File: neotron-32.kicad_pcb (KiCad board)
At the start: 2 copper layers, 166.9 x 140.7 mm, 93 parts, among them J1 Conn_02x06, J10 micro SD Card, J11 Conn_02x13_Top_Bottom, J12 AVR-ISP-6, J13 DE9 Male, J14 DE9 Male, J15 Double-mini-DIN-6, J17 DB15HD_Female, J18 Conn_02x05, J2 Conn_02x06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

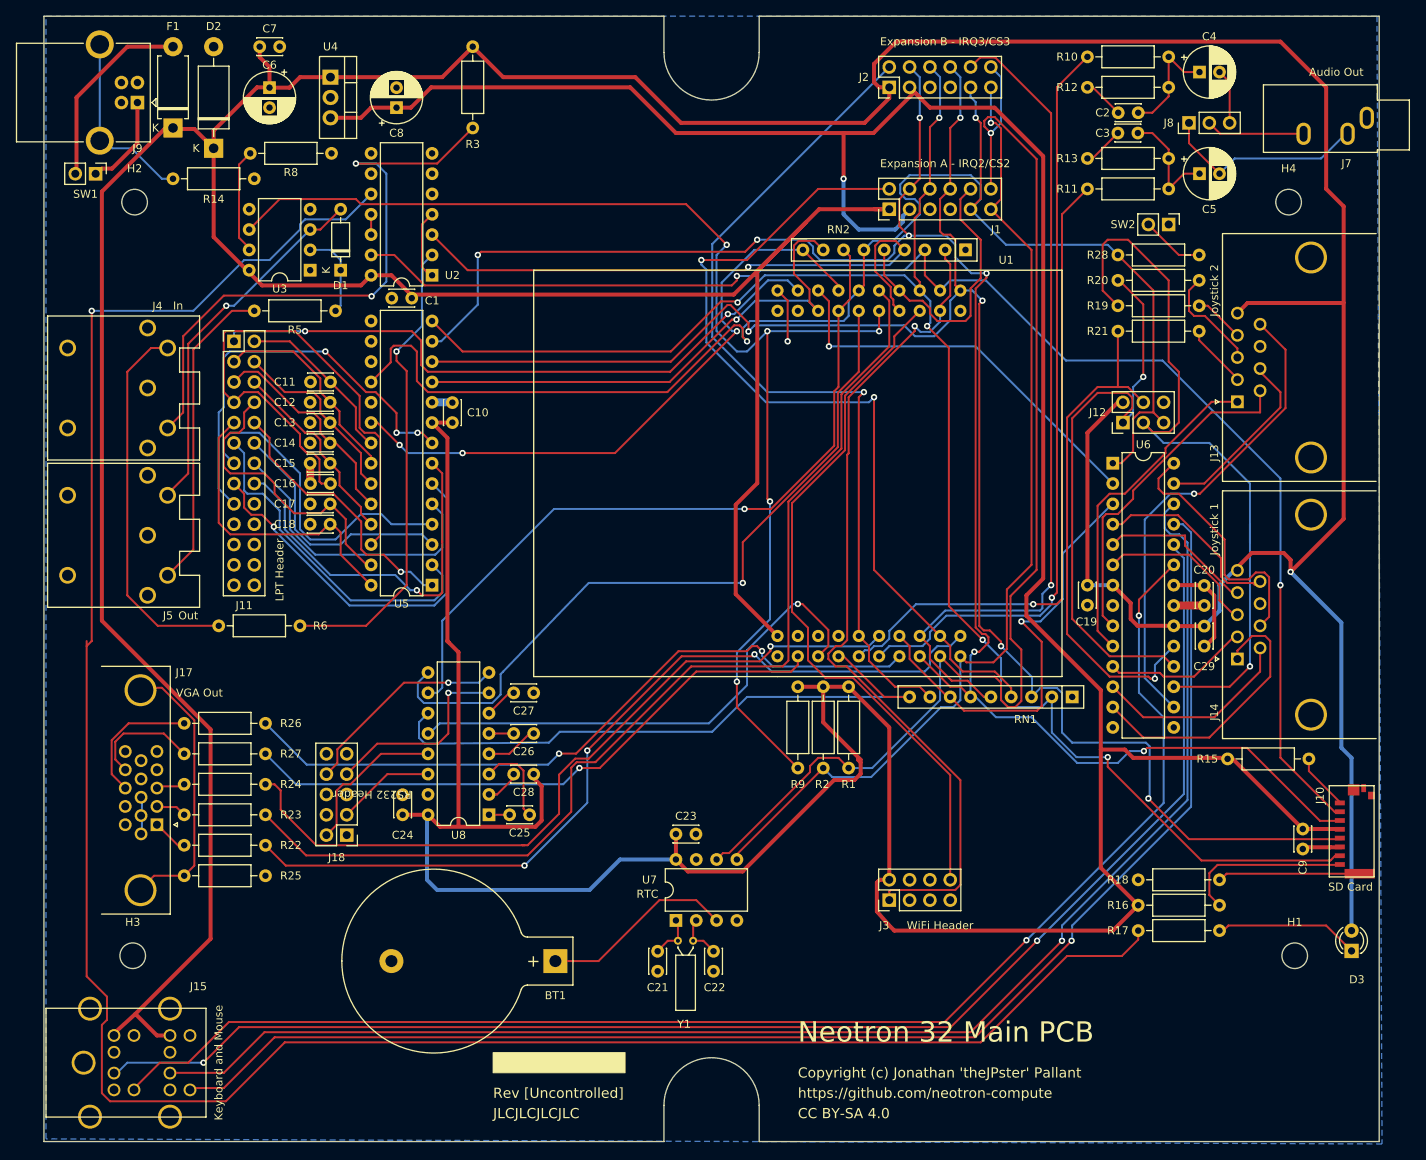
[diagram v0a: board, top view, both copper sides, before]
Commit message: Moved non-standard components into local libraries.
neotron-32.lib is the symbol library.
neotron-32.pretty is the footprint library.

Also swapped the DE9 and DB25 headers for IDC boxed versions. Involved
moving a resistor out of the way.

The Keystone 103 battery holder is a straight copy of the standard
footprint, but with the Courtyard removed to bypass the 'Courtyard is
not closed' DRC error.
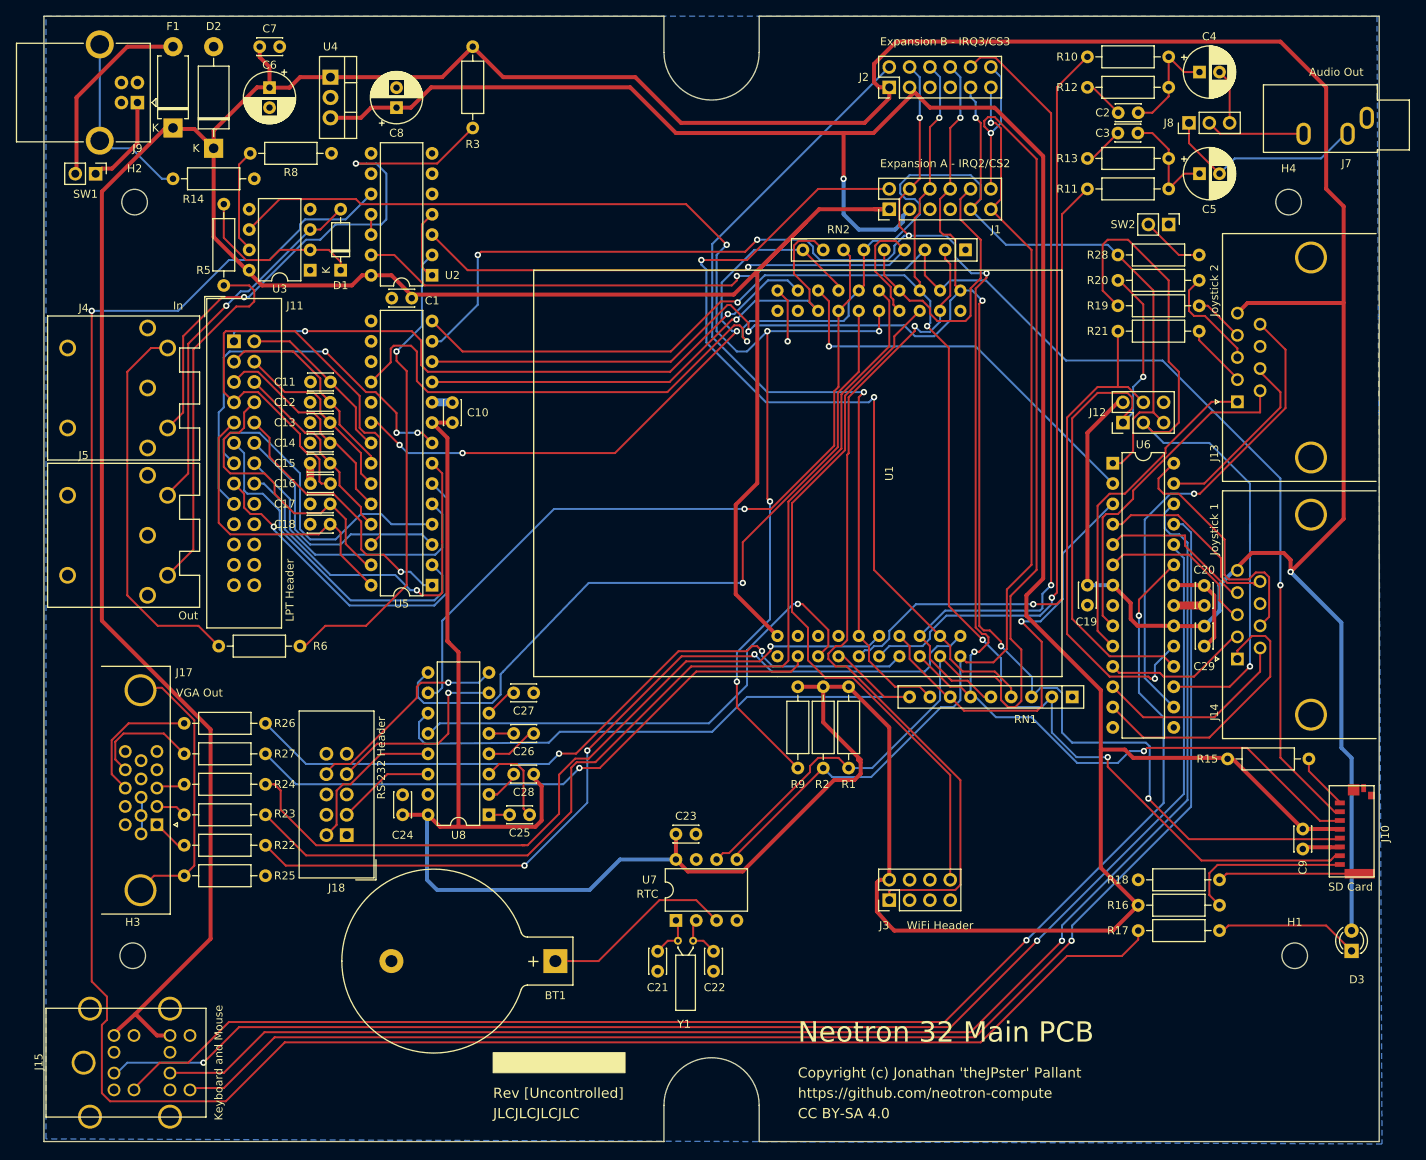
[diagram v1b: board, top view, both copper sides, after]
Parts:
- BT1: footprint JGP Footprints:BatteryHolder_Keystone_103_1x20mm -> Neotron 32:BatteryHolder_Keystone_103_1x20mm
- J10: footprint JGP Footprints:Molex_4730_2651 -> Neotron 32:Molex_4730_2651
- J11: footprint Connector_PinHeader_2.54mm:PinHeader_2x13_P2.54mm_Vertical -> Connector_IDC:IDC-Header_2x13_P2.54mm_Vertical
- J15: footprint JGP Footprints:Double_mini-DIN_6 -> Neotron 32:Double_mini-DIN_6
- J18: footprint Connector_PinHeader_2.54mm:PinHeader_2x05_P2.54mm_Vertical -> Connector_IDC:IDC-Header_2x05_P2.54mm_Vertical
- J4, J5: footprint JGP Footprints:5P180 DIN Socket -> Neotron 32:5P180_DIN_Socket
- U1: footprint JGP Footprints:Launchpad_4x10 -> Neotron 32:Launchpad_4x10
- moved R5 19.3 mm to (93.3, 41.3), turned to 270 degrees
- moved R6 2.54 mm to (102.9, 96.5)
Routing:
- net Net-(D1-Pad1): track 10.9 -> 22.2 mm
- net Net-(J5-Pad4): track 39.2 -> 45.1 mm
- net Net-(J4-Pad4): track 74.7 -> 70.1 mm
- net Net-(R17-Pad2): track 280.8 -> 279.6 mm
- net Net-(J4-Pad5): track 47.2 -> 48.3 mm
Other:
- board text added: "RS-232 Header"
- board text removed: "RS232 Header"

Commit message: Add a push button power switch.
Also moved reset into the corner and tidied up a few tracks.
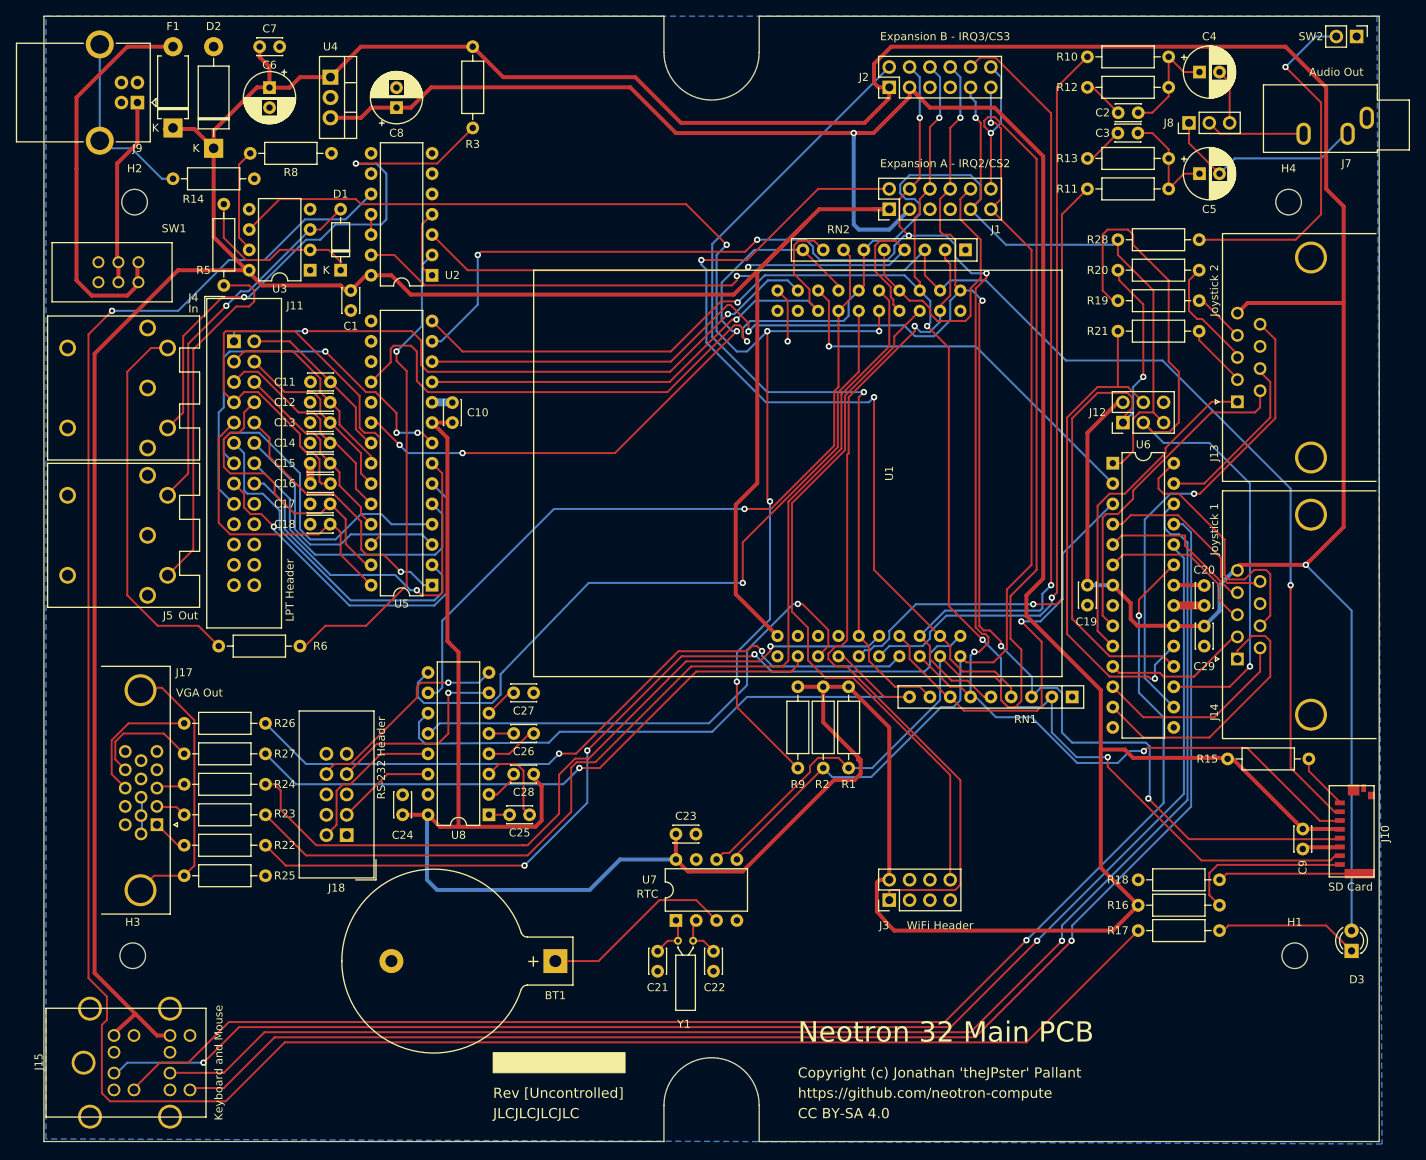
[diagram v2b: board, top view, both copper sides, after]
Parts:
- SW1: value SW_SPST -> SW_Push_DPDT; footprint Connector_PinHeader_2.54mm:PinHeader_1x02_P2.54mm_Vertical -> Neotron 32:PHB2UEETS1A
- moved SW2 33.2 mm to (234.9, 20.3)
- moved SW1 12.5 mm to (79.4, 49.8), turned to 0 degrees
- moved C1 7.68 mm to (109.2, 52.1), turned to 270 degrees
- moved R28 1.91 mm to (205.1, 45.7)
- moved R20 1.27 mm to (215.3, 49.5)
- moved R19 0.63 mm to (215.3, 53.3)
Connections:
- SW1 pad 1: Net-(J9-Pad1) -> (no net)
- SW1 pad 2: Net-(F1-Pad2) -> Net-(J9-Pad1)
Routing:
- net Net-(R28-Pad2): track 7.93 -> 44.7 mm, vias 0 -> 1
- net Net-(F1-Pad2): track 24.9 -> 50.0 mm
- net +5V: track 658.1 -> 641.0 mm
- net Net-(J9-Pad1): track 11.7 -> 23.6 mm
- net GND: track 45.1 -> 36.4 mm
- net /Keyboard, Mouse and Joystick/AT_SCK: track 94.9 -> 97.5 mm
- net Net-(R17-Pad2): track 279.6 -> 277.5 mm
- net /~RESET: track 183.6 -> 185.2 mm
- net +3V3: track 496.4 -> 497.9 mm
- net /Keyboard, Mouse and Joystick/AT_MISO: track 71.5 -> 72.7 mm
- net /Keyboard, Mouse and Joystick/SELECT_JS2: track 22.8 -> 21.7 mm
- net /Keyboard, Mouse and Joystick/START_C_JS2: track 60.1 -> 59.1 mm
- net /Keyboard, Mouse and Joystick/LEFT_GND_JS2: track 13.5 -> 14.3 mm
- net /Keyboard, Mouse and Joystick/SELECT_JS1: track 32.2 -> 32.9 mm

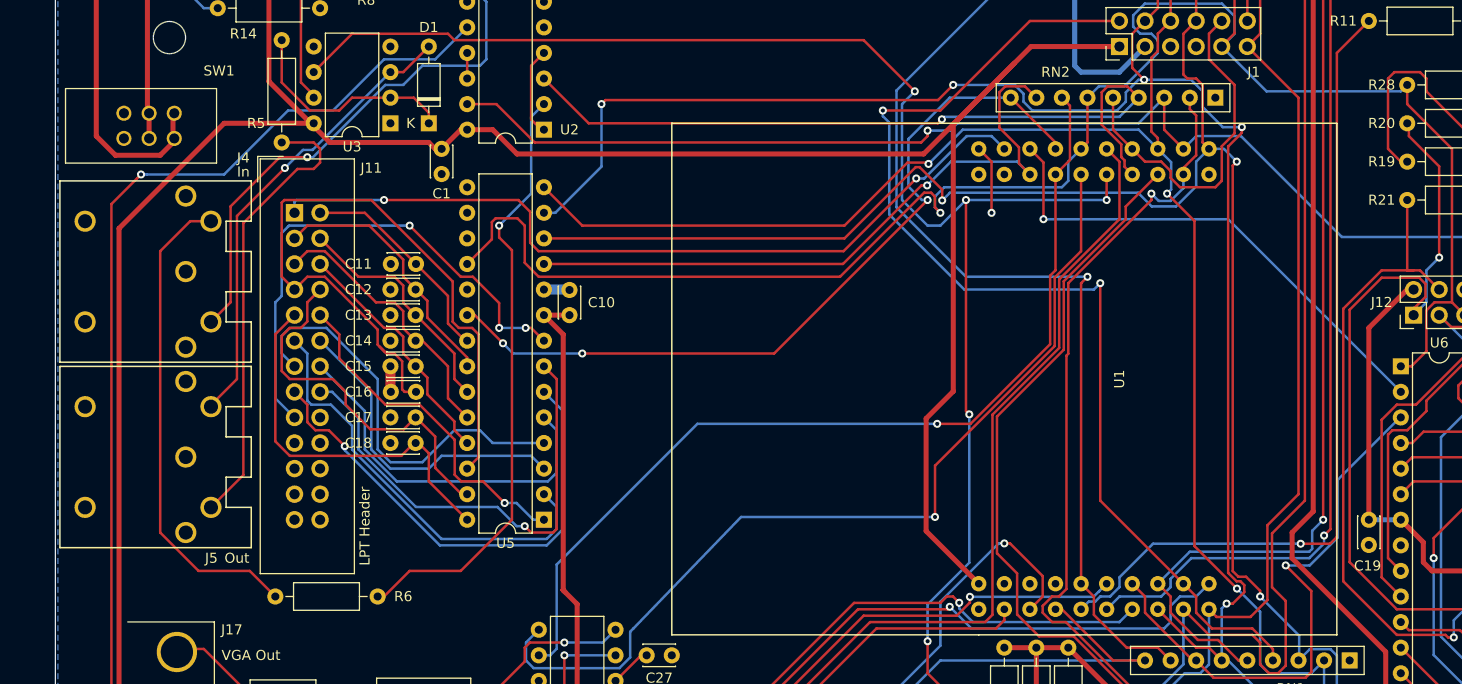
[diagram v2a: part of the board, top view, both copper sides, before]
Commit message: Fixed spacing between MIDI connectors.
Also tidied up some more tracks and re-aligned end panel.
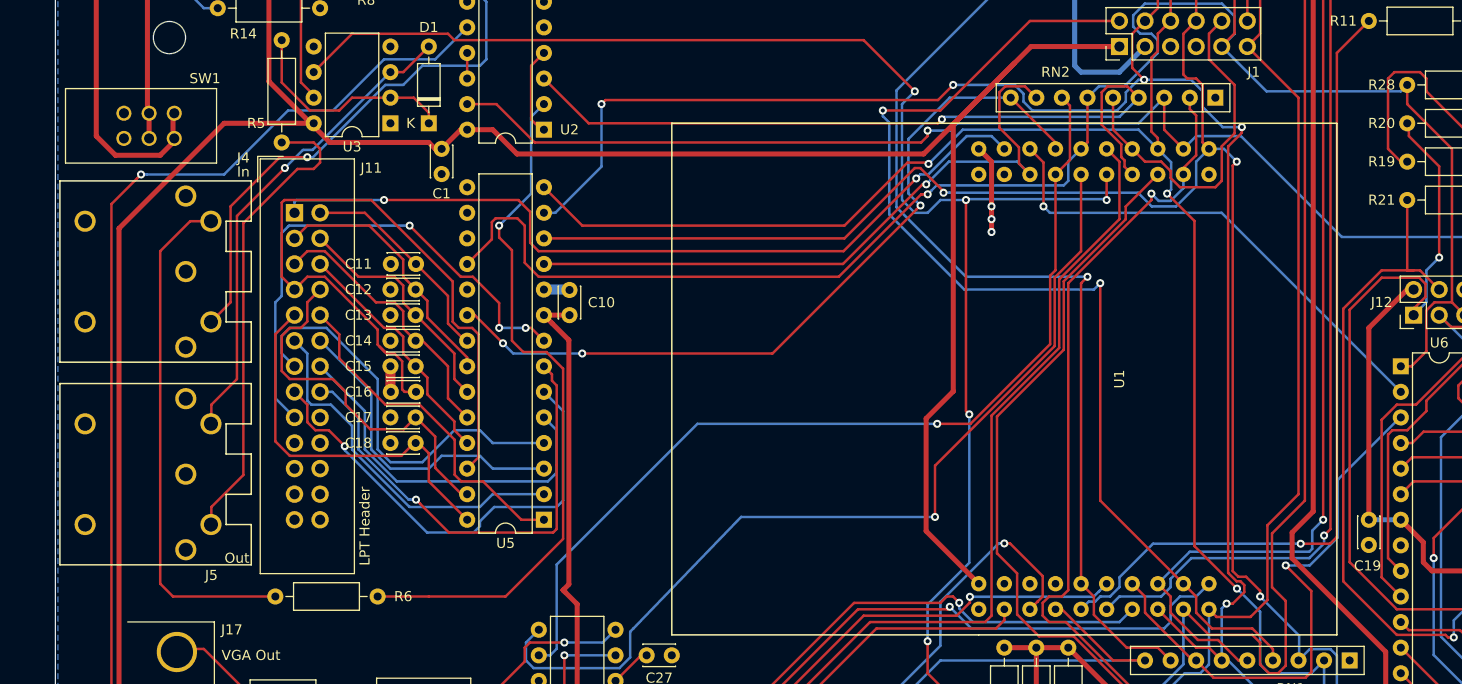
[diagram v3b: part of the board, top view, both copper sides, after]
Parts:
- moved J5 1.70 mm to (78.8, 84.4)
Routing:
- net Net-(R6-Pad1): track 59.5 -> 69.1 mm
- net /Parallel Printer/~BUSY: track 42.7 -> 36.2 mm
- net /~RESET: track 185.2 -> 181.3 mm
- net Net-(J4-Pad5): track 48.3 -> 51.2 mm
- net /Parallel Printer/ERROR: track 49.3 -> 46.9 mm
- net Net-(D1-Pad2): track 45.8 -> 47.7 mm
- net GND: track 36.4 -> 38.3 mm, vias 1 -> 3
- net /PA2_SPI_CLK: track 216.9 -> 215.6 mm
- net Net-(J5-Pad4): track 45.1 -> 46.3 mm
- net /~PF0_IRQ1: track 80.3 -> 79.3 mm
- net /PC6_MIDI_IN: track 159.5 -> 158.6 mm
- net /PE0_U7RX: track 50.1 -> 49.4 mm
- net /PD7_U2TX: track 106.5 -> 107.0 mm
- net /Parallel Printer/ACK: track 34.1 -> 34.4 mm, vias 1 -> 0
